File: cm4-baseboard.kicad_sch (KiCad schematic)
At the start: 4 parts

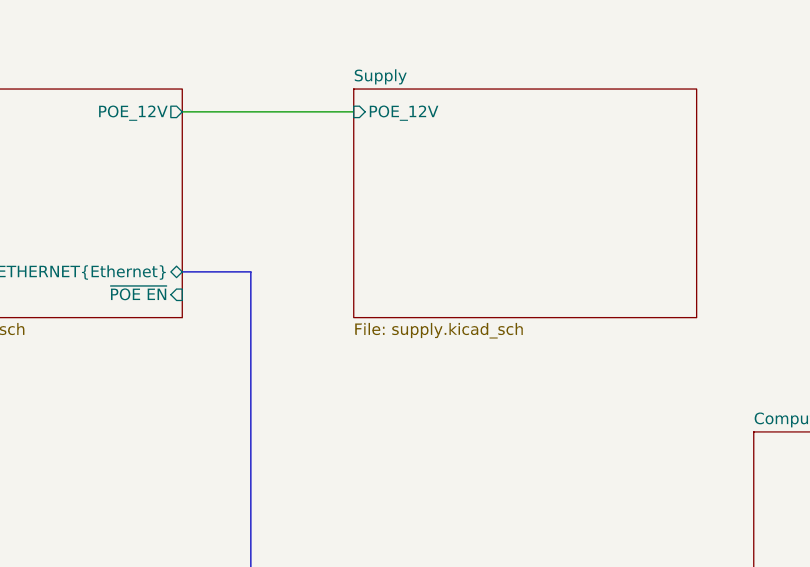
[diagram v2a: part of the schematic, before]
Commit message: [#53804] Clean SD&NVMe sch; Change NVMe to x4; Update 3V3 power sch
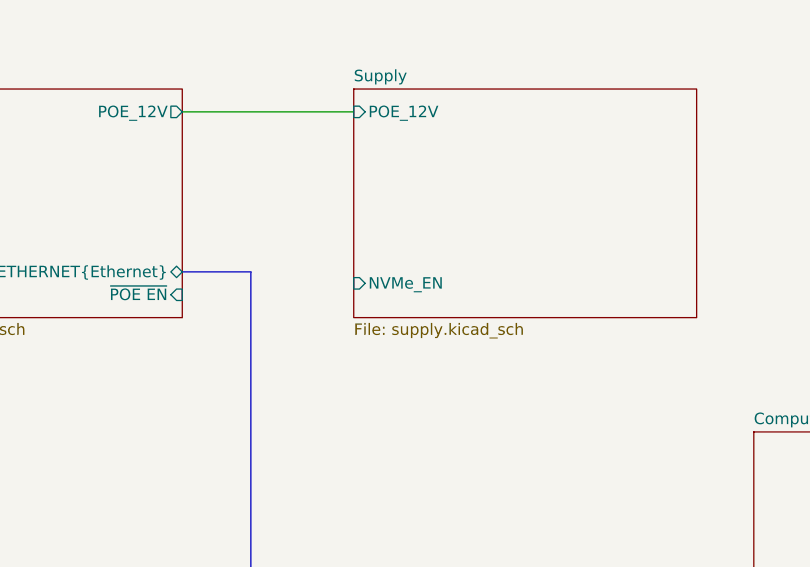
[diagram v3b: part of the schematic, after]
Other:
- sheet Supply ports: added NVMe_EN; removed none

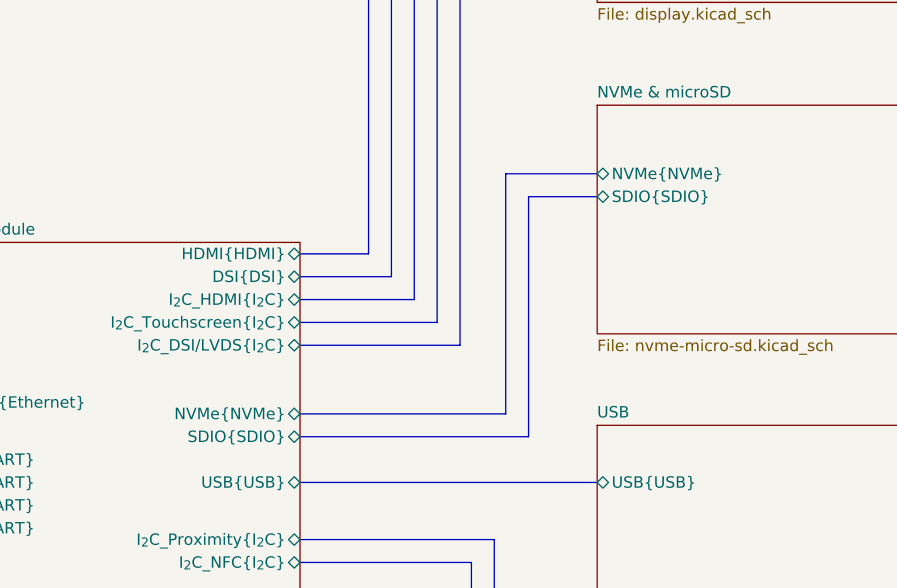
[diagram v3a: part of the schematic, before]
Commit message: [#53804] Visual cleanup for m.2/SD sch
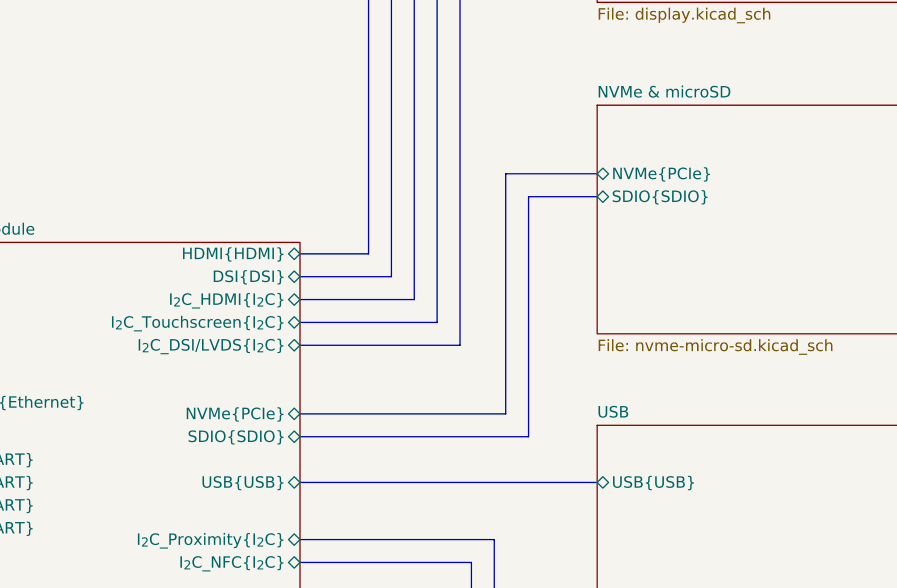
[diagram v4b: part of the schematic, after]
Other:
- sheet Compute module ports: added NVMe{PCIe}; removed NVMe{NVMe}
- sheet NVMe & microSD ports: added NVMe{PCIe}; removed NVMe{NVMe}
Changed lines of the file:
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@@
     (comment 1 "www.antmicro.com")
   )
+  (bus_alias "DSI" (members "D0_P" "D0_N" "D1_P" "D1_N" "D2_P" "D2_N" "D3_P" "D3_N" "CLK_P" "CLK_N"))
+  (bus_alias "UART" (members "TX" "RX"))
   (bus_alias "USB" (members "RX_P" "RX_N" "TX_P" "TX_N" "D_P" "D_N"))
+  (bus_alias "HDMI" (members "D0_P" "D0_N" "D1_P" "D1_N" "D2_P" "D2_N" "CLK_P" "CLK_N"))
+  (bus_alias "PCIe" (members "TX0_P" "TX0_N" "RX0_P" "RX0_N" "CLK_P" "CLK_N" "TX1_N" "TX2_N" "TX3_N" "TX1_P" "TX2_P" "TX3_P" "RX1_N" "RX2_N" "RX3_N" "RX1_P" "RX2_P" "RX3_P" "~{RST}" "~{CLK_REQ}"))
   (bus_alias "I_{2}C" (members "SCL" "SDA"))
   (bus_alias "CSI" (members "D0_P" "D0_N" "D1_P" "D1_N" "D2_P" "D2_N" "D3_P" "D3_N" "CLK_P" "CLK_N"))
-  (bus_alias "NVMe" (members "TX0_P" "TX0_N" "RX0_P" "RX0_N" "CLK_P" "CLK_N" "TX1_N" "TX2_N" "TX3_N" "TX1_P" "TX2_P" "TX3_P" "RX1_N" "RX2_N" "RX3_N" "RX1_P" "RX2_P" "RX3_P" "~{RST}" "~{CLK_REQ}"))
-  (bus_alias "HDMI" (members "D0_P" "D0_N" "D1_P" "D1_N" "D2_P" "D2_N" "CLK_P" "CLK_N"))
-  (bus_alias "UART" (members "TX" "RX"))
-  (bus_alias "DSI" (members "D0_P" "D0_N" "D1_P" "D1_N" "D2_P" "D2_N" "D3_P" "D3_N" "CLK_P" "CLK_N"))
   (bus_alias "SDIO" (members "D0" "D1" "D2" "D3" "CMD" "CLK" "CD"))
   (bus_alias "Ethernet" (members "D0_P" "D0_N" "D1_P" "D1_N" "D2_P" "D2_N" "D3_P" "D3_N" "LED_ACT" "LED_LINK"))
@@
       (effects (font (size 1.27 1.27)) (justify left))
     )
-    (pin "NVMe{NVMe}" bidirectional (at 243.84 120.65 0)
+    (pin "NVMe{PCIe}" bidirectional (at 243.84 120.65 0)
       (effects (font (size 1.27 1.27)) (justify right))
     )
@@
       (effects (font (size 1.27 1.27)) (justify left top))
     )
-    (pin "NVMe{NVMe}" bidirectional (at 276.86 93.98 180)
+    (pin "NVMe{PCIe}" bidirectional (at 276.86 93.98 180)
       (effects (font (size 1.27 1.27)) (justify left))
     )
@@
       (reference "#PWR?") (unit 1) (value "GND") (footprint "")
     )
+    (path "/00000000-0000-0000-0000-00005fea1b94/f1001aad-8cd7-4e0a-bbab-ed1980b0dd29"
+      (reference "#PWR?") (unit 1) (value "GND") (footprint "")
+    )
     (path "/00000000-0000-0000-0000-00005fea1b94/f4ce2705-9ab4-4e1a-98c2-271275337917"
       (reference "#PWR?") (unit 1) (value "GND") (footprint "")
@@
       (reference "C48") (unit 1) (value "C_1u_0603") (footprint "antmicro-footprints:C_0603_1608Metric")
     )
-    (path "/00000000-0000-0000-0000-00005fea1b94/00000000-0000-0000-0000-00005ffa31af"
-      (reference "C49") (unit 1) (value "C_100n_0603") (footprint "antmicro-footprints:C_0603_1608Metric")
-    )
-    (path "/00000000-0000-0000-0000-00005fea1b94/00000000-0000-0000-0000-00005ff80661"
-      (reference "C50") (unit 1) (value "C_100n_0603") (footprint "antmicro-footprints:C_0603_1608Metric")
-    )
-    (path "/00000000-0000-0000-0000-00005fea1b94/00000000-0000-0000-0000-00005ff8c54b"
-      (reference "C51") (unit 1) (value "C_100n_0603") (footprint "antmicro-footprints:C_0603_1608Metric")
-    )
-    (path "/00000000-0000-0000-0000-00005fea1b94/00000000-0000-0000-0000-00005ffa31bc"
-      (reference "C52") (unit 1) (value "C_1n_0603") (footprint "antmicro-footprints:C_0603_1608Metric")
-    )
-    (path "/00000000-0000-0000-0000-00005fea1b94/00000000-0000-0000-0000-00005ff829cf"
-      (reference "C53") (unit 1) (value "C_1n_0603") (footprint "antmicro-footprints:C_0603_1608Metric")
-    )
-    (path "/00000000-0000-0000-0000-00005fea1b94/00000000-0000-0000-0000-00005ff8c558"
-      (reference "C54") (unit 1) (value "C_1n_0603") (footprint "antmicro-footprints:C_0603_1608Metric")
-    )
     (path "/49e0afda-d892-4d16-b8c1-dc5863c48dfa/682cadd9-bbdc-4cac-adbc-c48513cfc838"

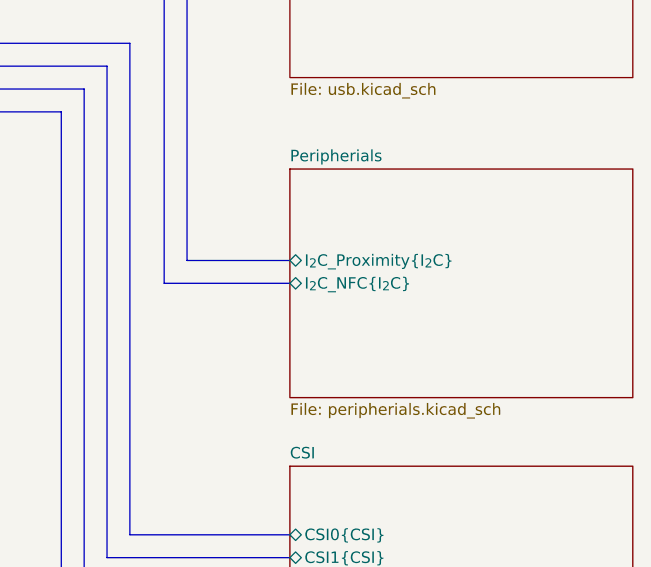
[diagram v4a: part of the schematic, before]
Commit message: [#54172] Peripherals: add passives to PN7160A, update PN7160A symbol
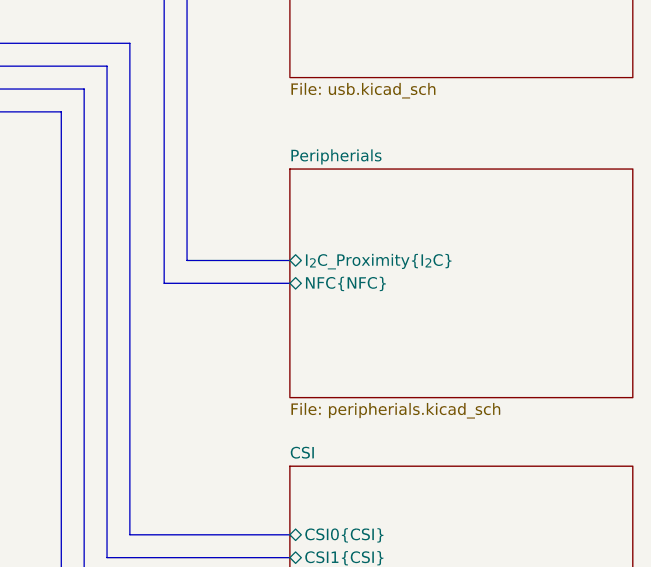
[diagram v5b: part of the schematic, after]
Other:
- sheet Peripherials ports: added NFC{NFC}; removed I_{2}C_NFC{I_{2}C}

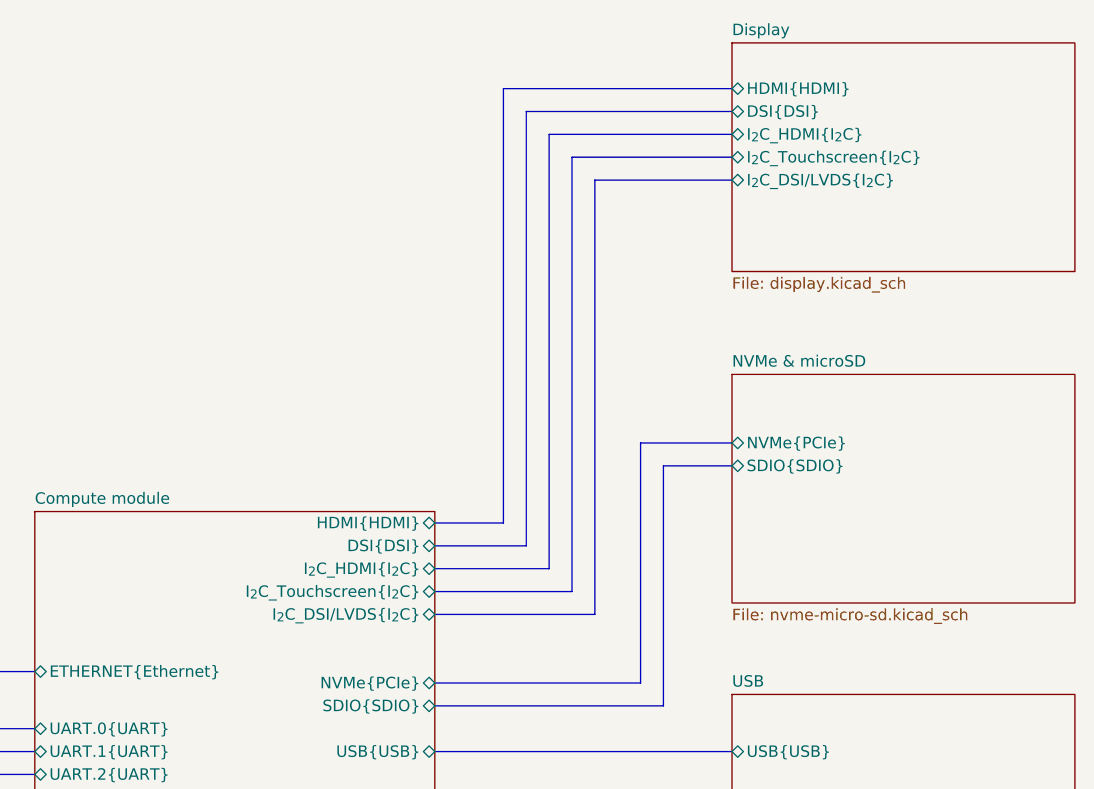
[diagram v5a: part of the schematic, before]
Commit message: [#54231] Add DSI connector; update hierarchic sch connections
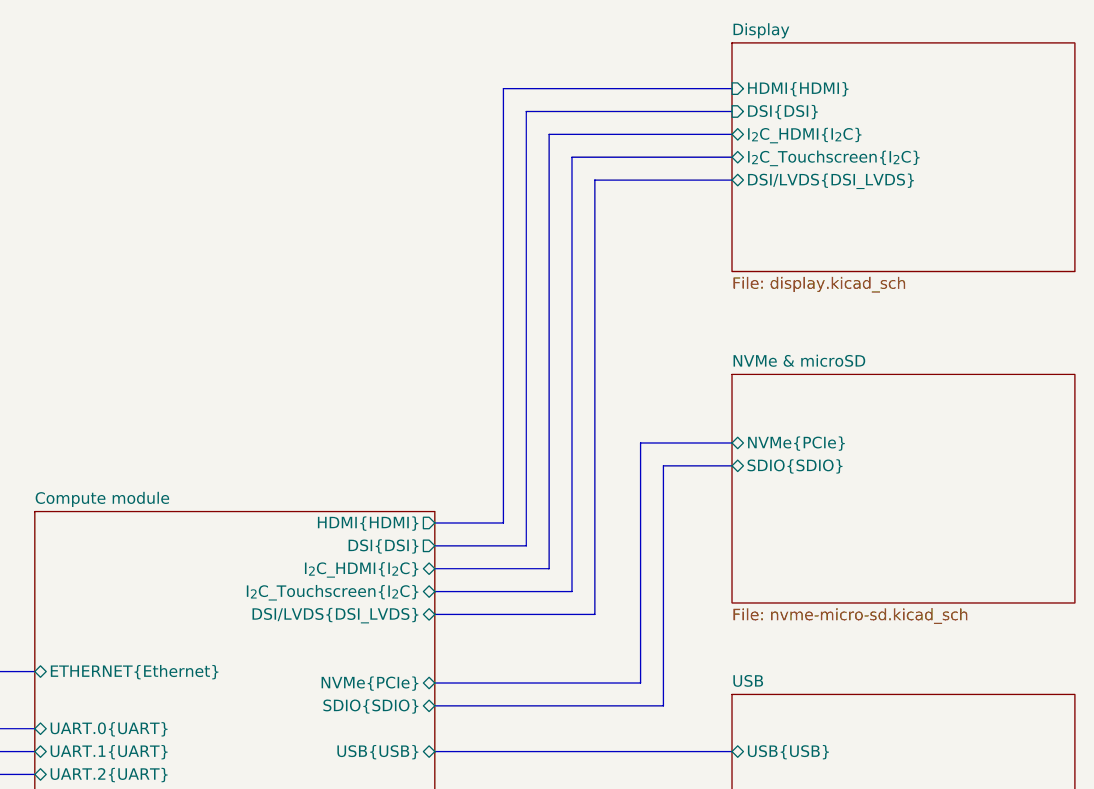
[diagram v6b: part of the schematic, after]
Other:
- sheet Compute module ports: added DSI/LVDS{DSI_LVDS}; removed I_{2}C_DSI/LVDS{I_{2}C}
- sheet Display ports: added DSI/LVDS{DSI_LVDS}; removed I_{2}C_DSI/LVDS{I_{2}C}

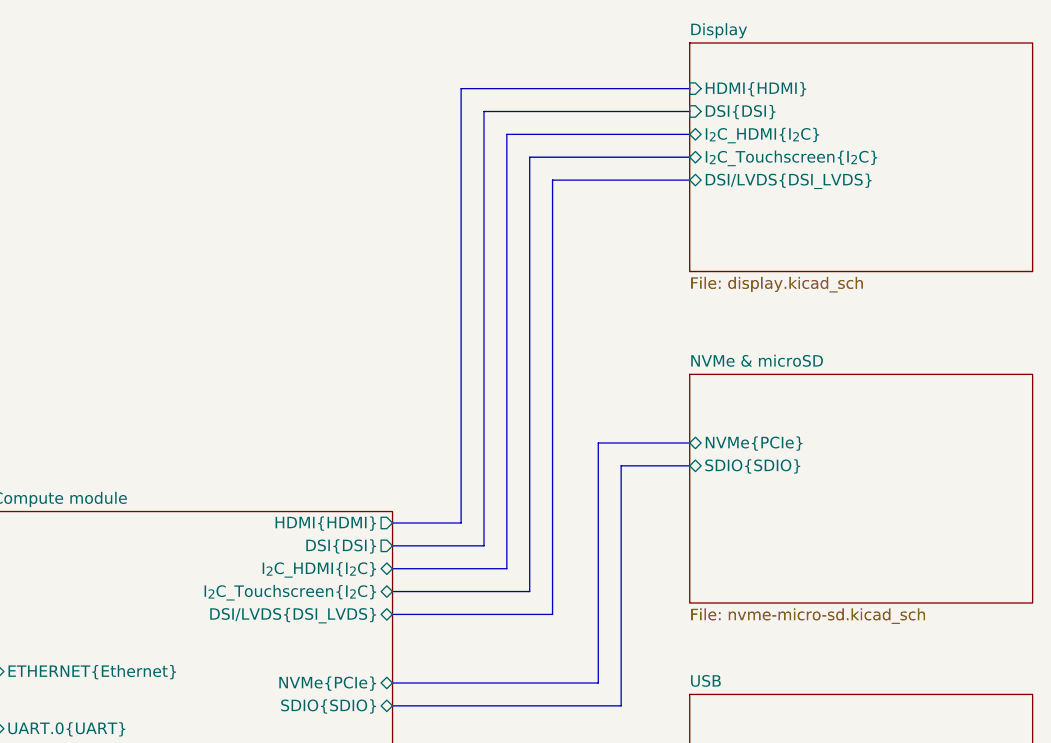
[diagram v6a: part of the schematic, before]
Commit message: [#54231] Clean HDMI connections
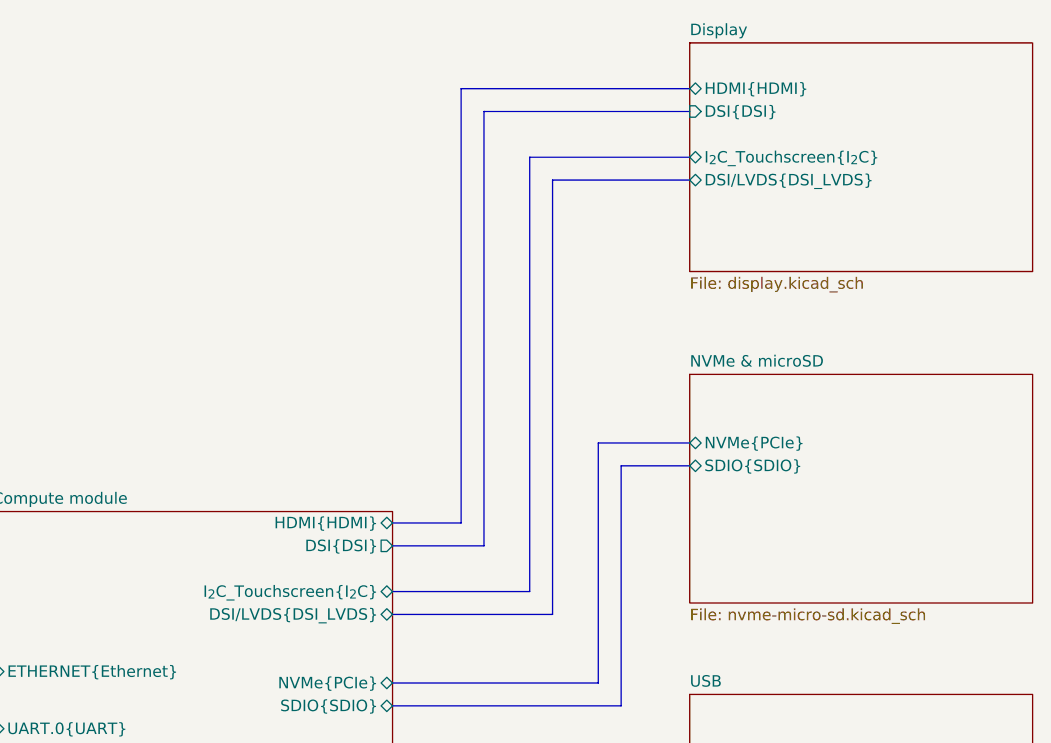
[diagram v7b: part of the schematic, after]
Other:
- sheet Compute module ports: added none; removed I_{2}C_HDMI{I_{2}C}
- sheet Display ports: added none; removed I_{2}C_HDMI{I_{2}C}
